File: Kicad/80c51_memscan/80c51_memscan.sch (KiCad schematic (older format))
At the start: 30 parts, among them J1 Conn_02x16_Male, J2 Conn_01x02_Male, SW1 SW_SPST, U1 P80C51FA-4N,112, Y1 4-12Mhz

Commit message: Changed the switch to be push button.
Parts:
- SW1: footprint Button_Switch_THT:SW_DIP_SPSTx01_Slide_9.78x4.72mm_W7.62mm_P2.54mm -> Button_Switch_SMD:SW_SPST_B3S-1000; symbol Switch:SW_SPST -> Switch:SW_Push
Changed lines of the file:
@@
 	3850 2750 4100 2750
 $Comp
-L Switch:SW_SPST SW1
+L Switch:SW_Push SW1
 U 1 1 5D7405E0
 P 1700 3250
 F 0 "SW1" V 1746 3162 50  0000 R CNN
 F 1 "SW_SPST" V 1655 3162 50  0000 R CNN
-F 2 "Button_Switch_THT:SW_DIP_SPSTx01_Slide_9.78x4.72mm_W7.62mm_P2.54mm" H 1700 3250 50  0001 C CNN
+F 2 "Button_Switch_SMD:SW_SPST_B3S-1000" H 1700 3250 50  0001 C CNN
 F 3 "" H 1700 3250 50  0001 C CNN
 	1    1700 3250

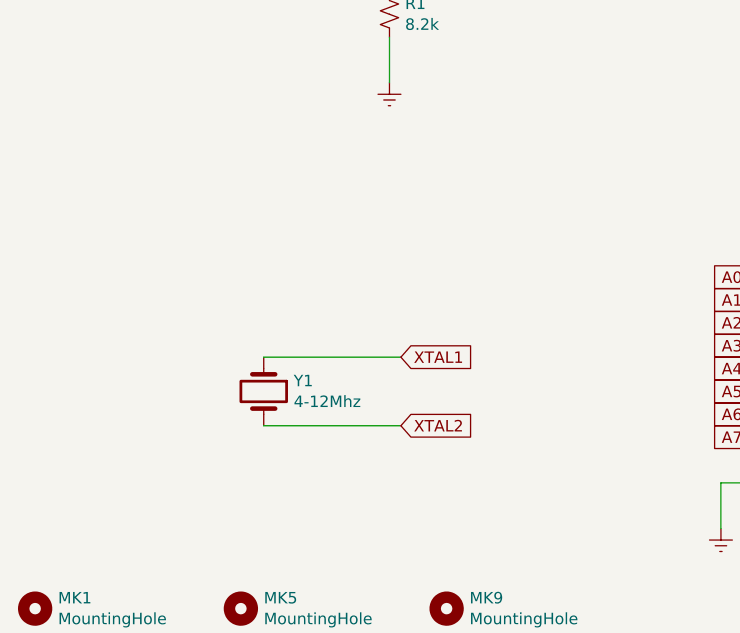
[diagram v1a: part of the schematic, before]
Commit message: Added caps to xtal.
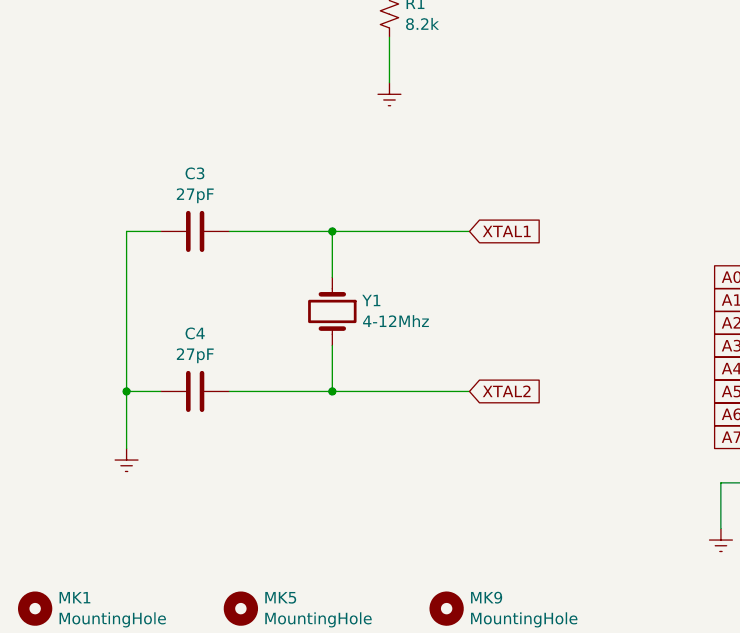
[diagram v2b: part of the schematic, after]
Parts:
- added C3, C4: 27pF, Capacitor_SMD:C_0603_1608Metric_Pad1.05x0.95mm_HandSolder, symbol Device:C
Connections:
- net Earth: now also C3.2, C4.2
- net XTAL1: now also C3.1
- net XTAL2: now also C4.1
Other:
- moved on the sheet: Y1
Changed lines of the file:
@@
 EESchema Schematic File Version 4
 LIBS:80c51_memscan-cache
-EELAYER 26 0
+EELAYER 30 0
 EELAYER END
 $Descr A4 11693 8268
@@
 L Device:Crystal Y1
 U 1 1 5D6AB8BC
-P 1950 5600
-F 0 "Y1" V 1904 5731 50  0000 L CNN
-F 1 "4-12Mhz" V 1995 5731 50  0000 L CNN
-F 2 "Crystal:Crystal_SMD_0603-2Pin_6.0x3.5mm_HandSoldering" H 1950 5600 50  0001 C CNN
-F 3 "~" H 1950 5600 50  0001 C CNN
-	1    1950 5600
-	0    1    1    0
-$EndComp
-Wire Wire Line
-	2550 5450 1950 5450
+P 2250 5250
+F 0 "Y1" V 2204 5381 50  0000 L CNN
+F 1 "4-12Mhz" V 2295 5381 50  0000 L CNN
+F 2 "Crystal:Crystal_SMD_0603-2Pin_6.0x3.5mm_HandSoldering" H 2250 5250 50  0001 C CNN
+F 3 "~" H 2250 5250 50  0001 C CNN
+	1    2250 5250
+	0    1    1    0
+$EndComp
+Wire Wire Line
+	2850 4900 2250 4900
 $Comp
 L Device:CP1_Small C1
@@
 $EndComp
 Wire Wire Line
-	1950 5750 2550 5750
+	2250 5600 2850 5600
 $Comp
 L power:+5V #PWR01
@@
 Text GLabel 4100 3400 0    50   Input ~ 0
 XTAL1
-Text GLabel 2550 5450 2    50   Input ~ 0
+Text GLabel 2850 4900 2    50   Input ~ 0
 XTAL1
-Text GLabel 2550 5750 2    50   Input ~ 0
+Text GLabel 2850 5600 2    50   Input ~ 0
 XTAL2
 Text GLabel 6100 3300 2    50   Input ~ 0
@@
 	1    0    0    -1
 $EndComp
+$Comp
+L Device:C C3
+U 1 1 5D74B625
+P 1650 4900
+F 0 "C3" V 1398 4900 50  0000 C CNN
+F 1 "27pF" V 1489 4900 50  0000 C CNN
+F 2 "Capacitor_SMD:C_0603_1608Metric_Pad1.05x0.95mm_HandSolder" H 1688 4750 50  0001 C CNN
+F 3 "~" H 1650 4900 50  0001 C CNN
+	1    1650 4900
+	0    1    1    0
+$EndComp
+Wire Wire Line
+	2250 4900 2250 5100
+Wire Wire Line
+	2250 5400 2250 5600
+Wire Wire Line
+	2250 4900 1800 4900
+Connection ~ 2250 4900
+Wire Wire Line
+	1500 4900 1350 4900
+Wire Wire Line
+	1350 4900 1350 5600
+$Comp
+L Device:C C4
+U 1 1 5D758C3B
+P 1650 5600
+F 0 "C4" V 1398 5600 50  0000 C CNN
+F 1 "27pF" V 1489 5600 50  0000 C CNN
+F 2 "Capacitor_SMD:C_0603_1608Metric_Pad1.05x0.95mm_HandSolder" H 1688 5450 50  0001 C CNN
+F 3 "~" H 1650 5600 50  0001 C CNN
+	1    1650 5600
+	0    1    1    0
+$EndComp
+Wire Wire Line
+	1350 5600 1500 5600
+Connection ~ 1350 5600
+Wire Wire Line
+	1800 5600 2250 5600
+Connection ~ 2250 5600
+Wire Wire Line
+	1350 5600 1350 5850
+$Comp
+L power:Earth #PWR013
+U 1 1 5D76155F
+P 1350 5850
+F 0 "#PWR013" H 1350 5600 50  0001 C CNN
+F 1 "Earth" H 1350 5700 50  0001 C CNN
+F 2 "" H 1350 5850 50  0001 C CNN
+F 3 "~" H 1350 5850 50  0001 C CNN
+	1    1350 5850
+	1    0    0    -1
+$EndComp
